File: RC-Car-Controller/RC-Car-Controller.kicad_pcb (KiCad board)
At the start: 4 copper layers, 138.8 x 77 mm, 122 parts, among them J1 Conn_01x02, J2 2171790001, J3 MCU_IF, J4 RF_IF, J5 ANT_IF, J6 Conn_01x08_Pin, Q1 DMG2301L, SW1 SW_Push, SW2 SW_SPDT, SW3 1825027-8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

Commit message: Changed
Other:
- board text added: "Rev.1"
- board text removed: "V1"
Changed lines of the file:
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@@
 		)
 	)
-	(gr_text "V1"
-		(at 202.946 117.983 0)
+	(gr_text "Rev.1"
+		(at 130.81 106.553 0)
 		(layer "F.SilkS")
 		(effects
@@
 			(justify left bottom)
 		)
-		(render_cache "V1" 0
+		(render_cache "Rev.1" 0
 			(polygon
 				(pts
-					(xy 203.829416 117.5512) (xy 203.137076 114.891024) (xy 203.467116 114.891024) (xy 203.942945 116.742228)
-					(xy 203.973305 116.873409) (xy 204.000175 116.997087) (xy 204.01615 117.07537) (xy 204.039159 117.199666)
-					(xy 204.041585 117.229844) (xy 204.064179 117.101237) (xy 204.070122 117.073509) (xy 204.099279 116.9434)
-					(xy 204.128737 116.816029) (xy 204.147049 116.738506) (xy 204.608609 114.891024) (xy 204.93865 114.891024)
-					(xy 204.242587 117.5512)
+					(xy 132.091301 103.468581) (xy 132.223301 103.494705) (xy 132.34379 103.539488) (xy 132.377692 103.556562)
+					(xy 132.49057 103.631261) (xy 132.584389 103.723993) (xy 132.653139 103.823944) (xy 132.704502 103.937102)
+					(xy 132.736841 104.061771) (xy 132.750158 104.197951) (xy 132.750538 104.226569) (xy 132.741465 104.360803)
+					(xy 132.714246 104.484335) (xy 132.661935 104.610518) (xy 132.60537 104.699296) (xy 132.51753 104.797567)
+					(xy 132.417323 104.875325) (xy 132.30475 104.932571) (xy 132.236866 104.955511) (xy 132.794585 106.1212)
+					(xy 132.432905 106.1212) (xy 131.903724 104.987771) (xy 131.478766 104.987771) (xy 131.478766 106.1212)
+					(xy 131.159892 106.1212) (xy 131.159892 104.691851) (xy 131.478766 104.691851) (xy 131.96266 104.691851)
+					(xy 132.096777 104.676823) (xy 132.220178 104.626151) (xy 132.297043 104.564674) (xy 132.373029 104.45699)
+					(xy 132.411875 104.336668) (xy 132.421739 104.222846) (xy 132.409379 104.098868) (xy 132.367235 103.981525)
+					(xy 132.295182 103.884121) (xy 132.189388 103.806622) (xy 132.060912 103.764892) (xy 131.96266 103.756943)
+					(xy 131.478766 103.756943) (xy 131.478766 104.691851) (xy 131.159892 104.691851) (xy 131.159892 103.461024)
+					(xy 131.96266 103.461024)
 				)
 			)
 			(polygon
 				(pts
-					(xy 205.410136 117.5512) (xy 205.410136 117.25528) (xy 206.12481 117.25528) (xy 206.12481 115.219203)
-					(xy 205.41696 115.745283) (xy 205.41696 115.371816) (xy 206.037337 114.891024) (xy 206.446786 114.891024)
-					(xy 206.446786 117.25528) (xy 207.036144 117.25528) (xy 207.036144 117.5512)
+					(xy 134.16018 104.064044) (xy 134.295429 104.091602) (xy 134.417142 104.139464) (xy 134.525318 104.207631)
+					(xy 134.594298 104.268754) (xy 134.676003 104.367956) (xy 134.737639 104.480458) (xy 134.779208 104.606259)
+					(xy 134.800709 104.745359) (xy 134.803986 104.830816) (xy 134.803986 105.208005) (xy 133.578121 105.208005)
+					(xy 133.578121 105.394118) (xy 133.590116 105.520447) (xy 133.631021 105.639536) (xy 133.700956 105.737807)
+					(xy 133.805586 105.815305) (xy 133.934295 105.857035) (xy 134.033478 105.864984) (xy 134.159627 105.854777)
+					(xy 134.283426 105.817067) (xy 134.328777 105.7924) (xy 134.422144 105.702755) (xy 134.471464 105.580231)
+					(xy 134.792198 105.580231) (xy 134.763545 105.712798) (xy 134.713566 105.828847) (xy 134.631849 105.939659)
+					(xy 134.549631 106.011393) (xy 134.440135 106.076804) (xy 134.31761 106.123526) (xy 134.182058 106.151559)
+					(xy 134.052763 106.160758) (xy 134.033478 106.160904) (xy 133.906775 106.153379) (xy 133.771526 106.12558)
+					(xy 133.649813 106.077298) (xy 133.541637 106.008533) (xy 133.472657 105.946874) (xy 133.390953 105.845755)
+					(xy 133.329316 105.729674) (xy 133.287747 105.598631) (xy 133.268089 105.474401) (xy 133.262969 105.362479)
+					(xy 133.262969 104.85501) (xy 133.264512 104.827093) (xy 133.578121 104.827093) (xy 133.578121 104.930076)
+					(xy 134.488834 104.930076) (xy 134.488834 104.827093) (xy 134.477141 104.6953) (xy 134.43727 104.573698)
+					(xy 134.369101 104.476581) (xy 134.26607 104.400972) (xy 134.147561 104.36232) (xy 134.033478 104.352505)
+					(xy 133.907609 104.364622) (xy 133.781517 104.41115) (xy 133.697233 104.476581) (xy 133.624649 104.583741)
+					(xy 133.587543 104.707569) (xy 133.578121 104.827093) (xy 133.264512 104.827093) (xy 133.270341 104.72162)
+					(xy 133.292457 104.599221) (xy 133.336892 104.470316) (xy 133.401396 104.356373) (xy 133.472657 104.270615)
+					(xy 133.571163 104.187219) (xy 133.683207 104.124306) (xy 133.808787 104.081876) (xy 133.947904 104.05993)
+					(xy 134.033478 104.056585)
+				)
+			)
+			(polygon
+				(pts
+					(xy 135.964711 106.1212) (xy 135.282916 104.09629) (xy 135.629087 104.09629) (xy 136.083823 105.487795)
+					(xy 136.119427 105.60671) (xy 136.146481 105.70989) (xy 136.170676 105.819696) (xy 136.192389 105.71051)
+					(xy 136.224035 105.586301) (xy 136.253806 105.487795) (xy 136.70482 104.09629) (xy 137.047268 104.09629)
+					(xy 136.365474 106.1212)
+				)
+			)
+			(polygon
+				(pts
+					(xy 138.296707 106.160904) (xy 138.173097 106.140586) (xy 138.075233 106.079634) (xy 138.007011 105.972307)
+					(xy 137.990861 105.866845) (xy 138.014673 105.740237) (xy 138.075233 105.650333) (xy 138.18714 105.58161)
+					(xy 138.296707 105.565342) (xy 138.420162 105.58659) (xy 138.517561 105.650333) (xy 138.586285 105.760671)
+					(xy 138.602553 105.866845) (xy 138.578566 105.992403) (xy 138.517561 106.079634) (xy 138.406155 106.145348)
+				)
+			)
+			(polygon
+				(pts
+					(xy 139.668981 106.1212) (xy 139.668981 105.82528) (xy 140.383655 105.82528) (xy 140.383655 103.789203)
+					(xy 139.675805 104.315283) (xy 139.675805 103.941816) (xy 140.296182 103.461024) (xy 140.70563 103.461024)
+					(xy 140.70563 105.82528) (xy 141.294988 105.82528) (xy 141.294988 106.1212)
 				)
 			)
@@
 	)
 	(segment
+		(start 141.341128 46.872872)
+		(end 138.811 49.403)
+		(width 1.27)
+		(layer "F.Cu")
+		(net 22)
+	)
+	(segment
 		(start 167.513 54.5325)
 		(end 167.513 55.681)
@@
 	)
 	(segment
-		(start 118.745 49.53)
-		(end 112.522 55.753)
+		(start 168.402 46.872872)
+		(end 141.341128 46.872872)
 		(width 1.27)
 		(layer "F.Cu")
@@
 	)
 	(segment
-		(start 168.402 46.872872)
-		(end 141.341128 46.872872)
+		(start 118.872 49.403)
+		(end 112.522 55.753)
 		(width 1.27)
 		(layer "F.Cu")
@@
 	)
 	(segment
-		(start 117.221 78.867)
-		(end 117.475 78.613)
-		(width 1.016)
+		(start 138.811 49.403)
+		(end 118.872 49.403)
+		(width 1.27)
 		(layer "F.Cu")
 		(net 22)
 	)
 	(segment
-		(start 141.341128 46.872872)
-		(end 138.684 49.53)
-		(width 1.27)
+		(start 117.221 78.867)
+		(end 117.475 78.613)
+		(width 1.016)
 		(layer "F.Cu")
 		(net 22)
@@
 		(layer "F.Cu")
 		(net 22)
-	)
-	(segment
-		(start 138.684 49.53)
-		(end 118.745 49.53)
-		(width 1.27)
-		(layer "F.Cu")
-		(net 22)

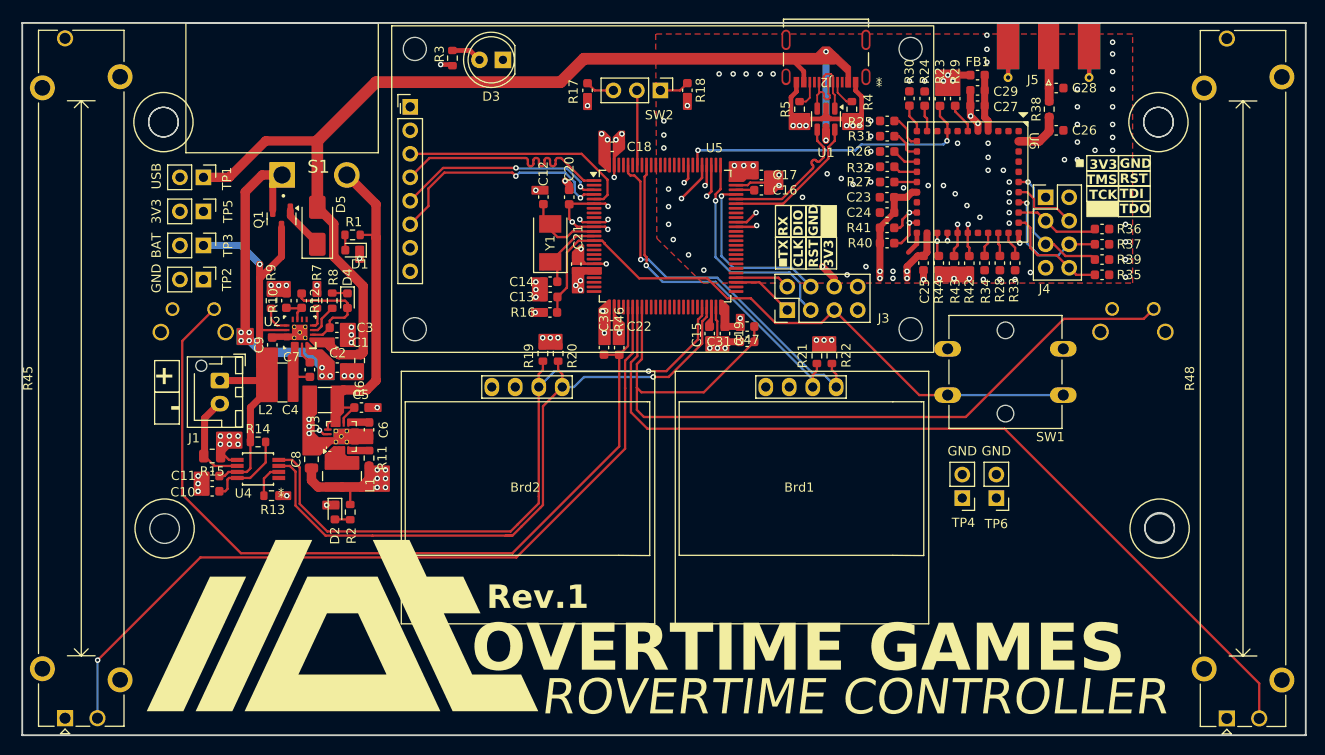
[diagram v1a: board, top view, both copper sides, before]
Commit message: Fixed GPIOADC
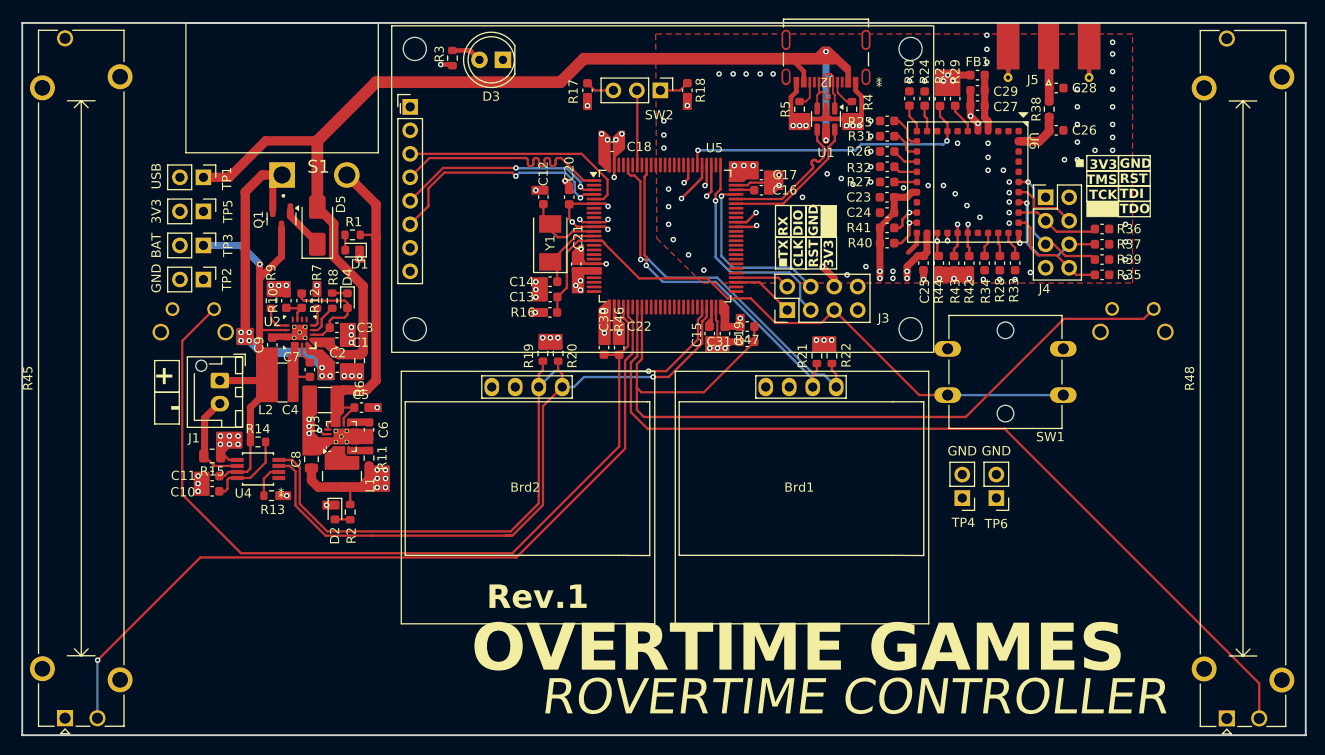
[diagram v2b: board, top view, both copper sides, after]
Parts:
- removed ? (x3): , 
- removed REF** (x4): MountingHole_3.2mm_M3, MountingHole:MountingHole_3.2mm_M3
- removed REF**: Overtime_Large, _LOGOS:Overtime_Large
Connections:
- U5 pad 29: unconnected-(U5-PA5-Pad29) -> /Inputs/Button_L
- U5 pad 30: /Inputs/Button_L -> /Inputs/Slider_L
- U5 pad 31: /Inputs/Slider_L -> unconnected-(U5-PA7-Pad31)
